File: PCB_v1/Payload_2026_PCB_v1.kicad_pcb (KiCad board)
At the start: 2 copper layers, 60 x 60 mm, 10 parts, among them J1 SD Card Reader, J2 Ozone Sensor, J3 SGP40 VOC Sensor, J4 IMU, J5 BME/BMP280, J6 Ultrasonic 1, J7 Ultrasonic 2, J8 Ultrasonic 3, J9 Battery

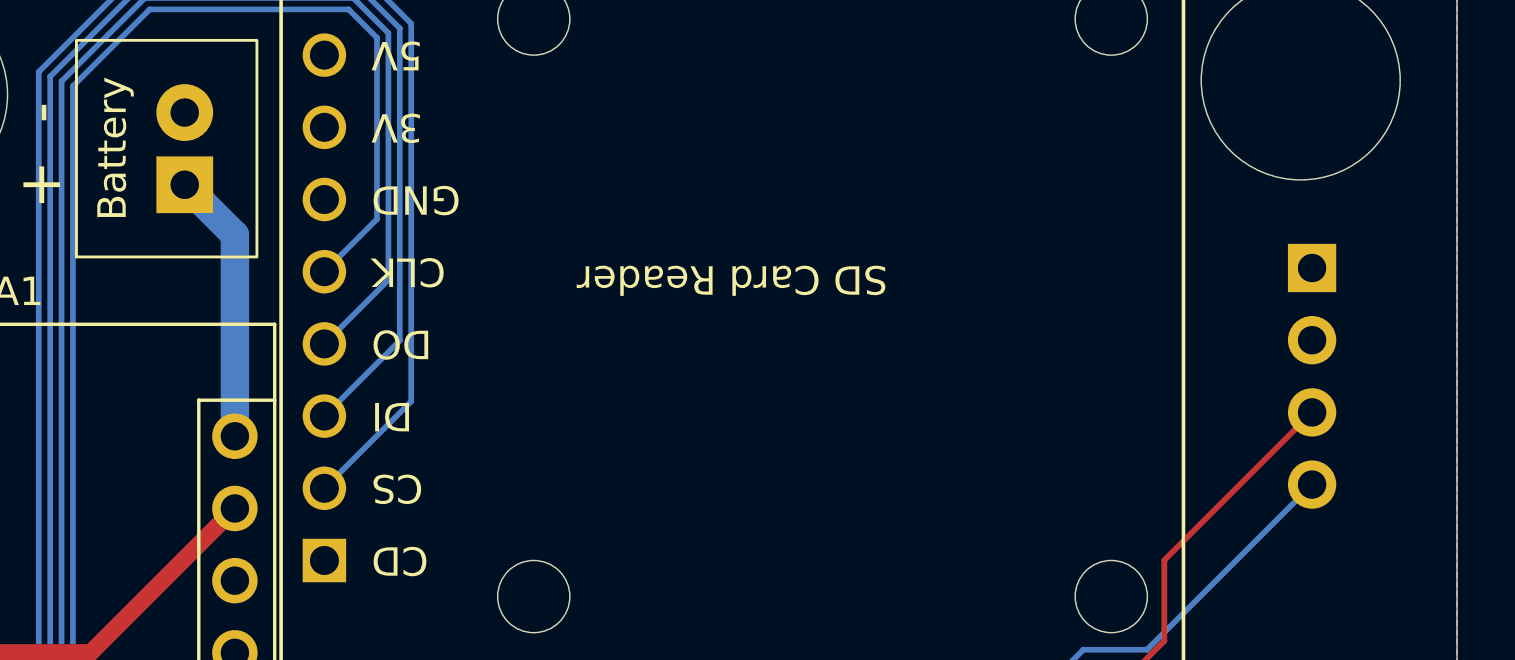
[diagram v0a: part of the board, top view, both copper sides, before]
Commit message: Set the VIN thickness on PCB
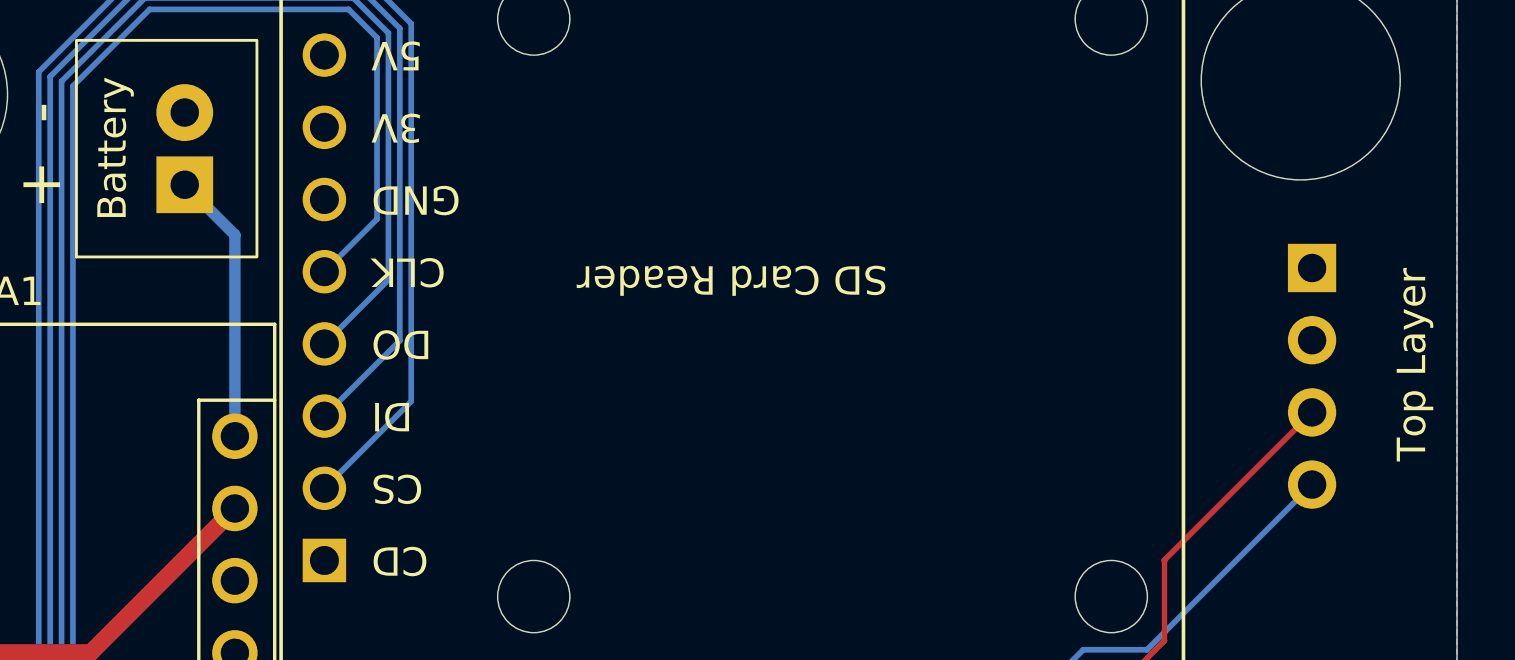
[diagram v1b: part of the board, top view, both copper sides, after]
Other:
- board text added: "Bottom Layer"
- board text added: "Top Layer"
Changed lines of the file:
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@@
+		)
+	)
+	(gr_text "Top Layer"
+		(at 79 35 90)
+		(layer "F.SilkS")
+		(effects
+			(font
+				(size 1 1)
+				(thickness 0.1)
+			)
+			(justify bottom)
 		)
 	)
@@
 		)
 	)
+	(gr_text "Bottom Layer"
+		(at 79 35 90)
+		(layer "B.SilkS")
+		(effects
+			(font
+				(size 1 1)
+				(thickness 0.1)
+			)
+			(justify bottom mirror)
+		)
+	)
 	(gr_text "Payload 2026"
 		(at 31 54 90)
@@
 		(start 37 37.52)
 		(end 37 30.435)
-		(width 1)
+		(width 0.4)
 		(layer "B.Cu")
 		(net 4)
@@
 		(start 37 30.435)
 		(end 35.235 28.67)
-		(width 1)
+		(width 0.4)
 		(layer "B.Cu")
 		(net 4)

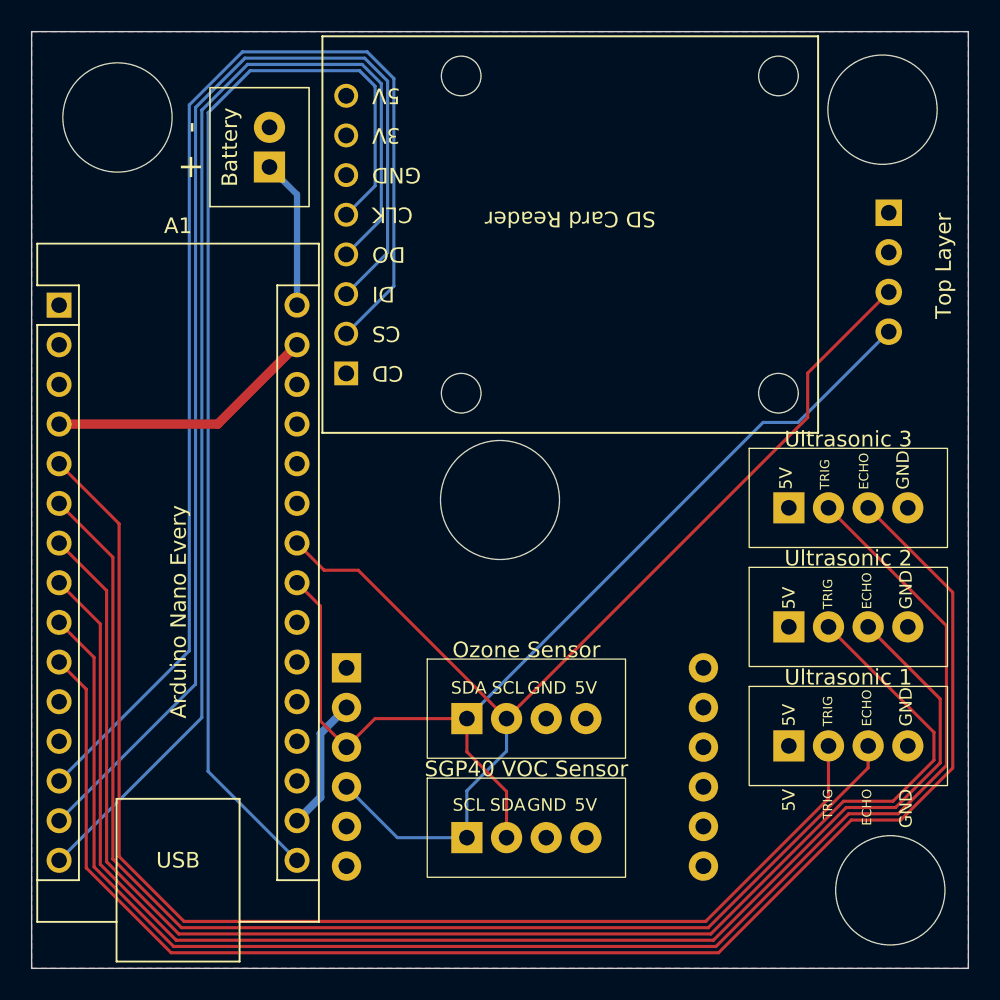
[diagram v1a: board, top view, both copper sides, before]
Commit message: Add SW-18020P to the PCB; generate gerber files
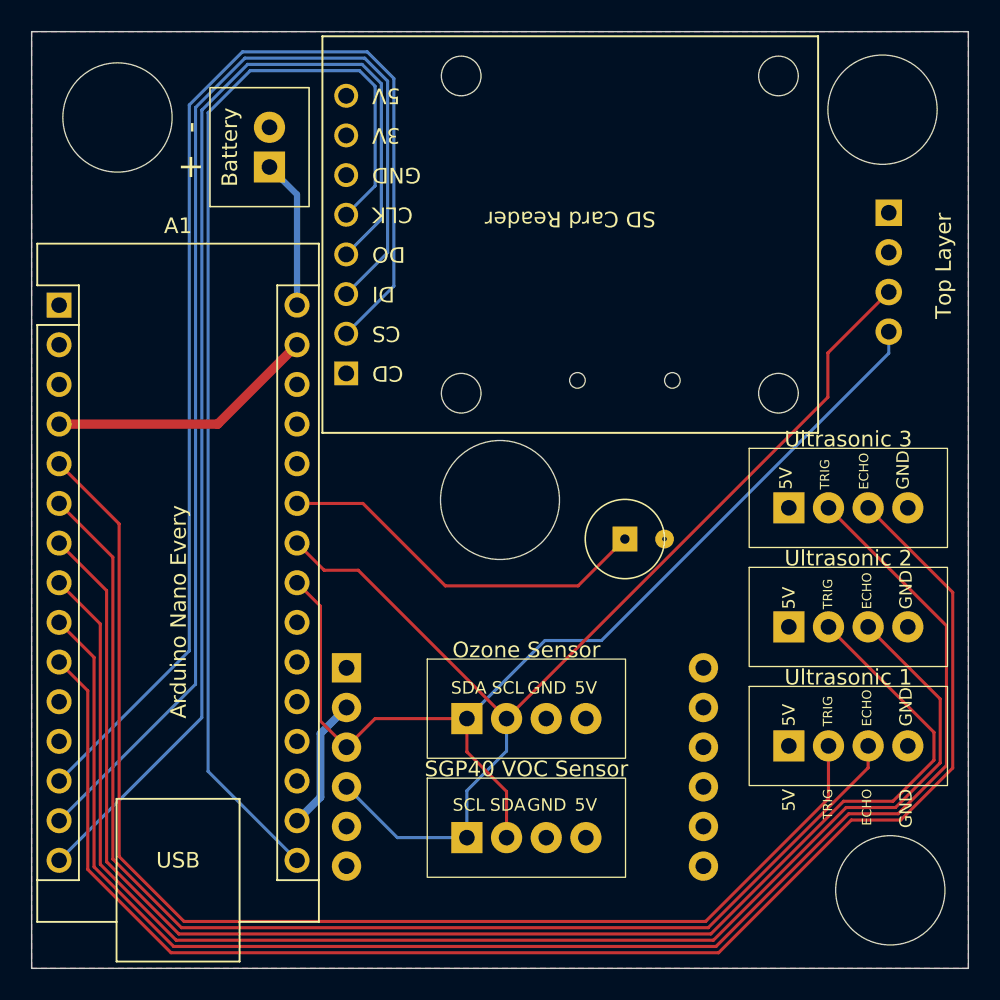
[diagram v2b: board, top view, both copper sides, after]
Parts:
- added ?: , clipboard:37f68170-0016-4afd-9e88-46bdadb5b772, F.Cu at (60.5, 47.0)
- added J10: SW-18020P, Payload_2026_PCB_v1:SW_18020P, F.Cu at (58.0, 52.5)
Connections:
- A1 pad 25: unconnected-(A1-A6-Pad25) -> /SW_18020P
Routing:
- net /SW_18020P: track 0.00 -> 24.4 mm
- net /SDA: track 66.3 -> 67.1 mm
